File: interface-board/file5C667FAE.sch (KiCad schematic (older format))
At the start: 24 parts

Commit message: interface-board getting there schematic-wise.
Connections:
- net labels added: 12V_IN
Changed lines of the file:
@@
 $Descr A4 11693 8268
 encoding utf-8
-Sheet 4 4
+Sheet 4 5
 Title ""
 Date ""
@@
 Connection ~ 6900 5350
 Text HLabel 8550 3400 0    50   Input ~ 0
-12V_OUT
+12V_IN
 Wire Wire Line
 	8550 3400 8600 3400

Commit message: schematic almost done maybe hopefully
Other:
- note added: "Fix all the HV/LV interface shit"
- moved on the sheet: C?, U?
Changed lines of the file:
@@
 Wire Wire Line
 	5700 3850 5900 3850
-Wire Notes Line
-	3350 4000 3350 2500
 Text Notes 6000 2950 0    50   ~ 0
 Pull high to disable
@@
 Text Notes 4350 2750 0    100  ~ 0
 HV-Interface
-Wire Notes Line width 39 rgb(255, 0, 0)
-	5400 1050 5400 6150
-Text Notes 3500 3800 0    118  ~ 24
+Text Notes 3350 3700 0    118  ~ 24
 HV\nDanger!
 $Comp
@@
 	7400 4750 7400 5800
 Wire Notes Line
-	6000 5800 7300 5800
-Wire Notes Line
-	6100 4750 7400 4750
-Wire Notes Line
 	3300 6200 3300 4650
-Wire Notes Line width 39 rgb(255, 0, 0)
-	5400 1150 3400 1150
 Text Notes 3850 1550 0    50   ~ 0
 May want to change value
@@
 L Regulator_Switching:R-78E5.0-0.5 U?
 U 1 1 5C66BF9B
-P 9050 3400
+P 9000 3550
 AR Path="/5C66BF9B" Ref="U?"  Part="1"
 AR Path="/5C667FAF/5C66BF9B" Ref="U?"  Part="1"
-F 0 "U?" H 9050 3642 50  0000 C CNN
-F 1 "R-78E5.0-0.5" H 9050 3551 50  0000 C CNN
-F 2 "Converter_DCDC:Converter_DCDC_RECOM_R-78E-0.5_THT" H 9100 3150 50  0001 L CIN
-F 3 "https://www.recom-power.com/pdf/Innoline/R-78Exx-0.5.pdf" H 9050 3400 50  0001 C CNN
-	1    9050 3400
-	1    0    0    -1
-$EndComp
-Wire Wire Line
-	8600 3400 8750 3400
-Wire Wire Line
-	9500 3400 9350 3400
+F 0 "U?" H 9000 3792 50  0000 C CNN
+F 1 "R-78E5.0-0.5" H 9000 3701 50  0000 C CNN
+F 2 "Converter_DCDC:Converter_DCDC_RECOM_R-78E-0.5_THT" H 9050 3300 50  0001 L CIN
+F 3 "https://www.recom-power.com/pdf/Innoline/R-78Exx-0.5.pdf" H 9000 3550 50  0001 C CNN
+	1    9000 3550
+	1    0    0    -1
+$EndComp
+Wire Wire Line
+	8550 3550 8700 3550
+Wire Wire Line
+	9450 3550 9300 3550
 $Comp
 L power:GND #PWR?
 U 1 1 5C66BFAA
-P 9050 3750
+P 9000 3900
 AR Path="/5C66BFAA" Ref="#PWR?"  Part="1"
 AR Path="/5C667FAF/5C66BFAA" Ref="#PWR?"  Part="1"
-F 0 "#PWR?" H 9050 3500 50  0001 C CNN
-F 1 "GND" H 9055 3577 50  0000 C CNN
-F 2 "" H 9050 3750 50  0001 C CNN
-F 3 "" H 9050 3750 50  0001 C CNN
-	1    9050 3750
-	1    0    0    -1
-$EndComp
-Wire Wire Line
-	9050 3750 9050 3700
-Wire Notes Line
-	8100 4050 8100 2750
-Text Notes 8150 2900 0    100  ~ 0
+F 0 "#PWR?" H 9000 3650 50  0001 C CNN
+F 1 "GND" H 9005 3727 50  0000 C CNN
+F 2 "" H 9000 3900 50  0001 C CNN
+F 3 "" H 9000 3900 50  0001 C CNN
+	1    9000 3900
+	1    0    0    -1
+$EndComp
+Wire Wire Line
+	9000 3900 9000 3850
+Text Notes 8100 3050 0    100  ~ 0
 12V->5V
 $Comp
 L Device:C C?
 U 1 1 5C66BFB3
-P 9500 3550
+P 9450 3700
 AR Path="/5C66BFB3" Ref="C?"  Part="1"
 AR Path="/5C667FAF/5C66BFB3" Ref="C?"  Part="1"
-F 0 "C?" H 9615 3596 50  0000 L CNN
-F 1 "0.1uF" H 9250 3450 50  0000 L CNN
-F 2 "Capacitor_SMD:C_0603_1608Metric" H 9538 3400 50  0001 C CNN
-F 3 "~" H 9500 3550 50  0001 C CNN
-	1    9500 3550
-	1    0    0    -1
-$EndComp
-Connection ~ 9500 3400
+F 0 "C?" H 9565 3746 50  0000 L CNN
+F 1 "0.1uF" H 9200 3600 50  0000 L CNN
+F 2 "Capacitor_SMD:C_0603_1608Metric" H 9488 3550 50  0001 C CNN
+F 3 "~" H 9450 3700 50  0001 C CNN
+	1    9450 3700
+	1    0    0    -1
+$EndComp
+Connection ~ 9450 3550
 $Comp
 L power:GND #PWR?
 U 1 1 5C66BFC5
-P 9650 3750
+P 9600 3900
 AR Path="/5C66BFC5" Ref="#PWR?"  Part="1"
 AR Path="/5C667FAF/5C66BFC5" Ref="#PWR?"  Part="1"
-F 0 "#PWR?" H 9650 3500 50  0001 C CNN
-F 1 "GND" H 9655 3577 50  0000 C CNN
-F 2 "" H 9650 3750 50  0001 C CNN
-F 3 "" H 9650 3750 50  0001 C CNN
-	1    9650 3750
-	1    0    0    -1
-$EndComp
-Wire Wire Line
-	9500 3700 9650 3700
-Wire Wire Line
-	9650 3700 9650 3750
-Connection ~ 9650 3700
-Wire Wire Line
-	9650 3700 9800 3700
+F 0 "#PWR?" H 9600 3650 50  0001 C CNN
+F 1 "GND" H 9605 3727 50  0000 C CNN
+F 2 "" H 9600 3900 50  0001 C CNN
+F 3 "" H 9600 3900 50  0001 C CNN
+	1    9600 3900
+	1    0    0    -1
+$EndComp
+Wire Wire Line
+	9450 3850 9600 3850
+Wire Wire Line
+	9600 3850 9600 3900
+Connection ~ 9600 3850
+Wire Wire Line
+	9600 3850 9750 3850
 $Comp
 L Device:C C?
 U 1 1 5C66BFCF
-P 8600 3550
+P 8550 3700
 AR Path="/5C66BFCF" Ref="C?"  Part="1"
 AR Path="/5C667FAF/5C66BFCF" Ref="C?"  Part="1"
-F 0 "C?" H 8715 3596 50  0000 L CNN
-F 1 "10uF" H 8715 3505 50  0000 L CNN
-F 2 "Capacitor_SMD:C_0603_1608Metric" H 8638 3400 50  0001 C CNN
-F 3 "~" H 8600 3550 50  0001 C CNN
-	1    8600 3550
+F 0 "C?" H 8665 3746 50  0000 L CNN
+F 1 "10uF" H 8665 3655 50  0000 L CNN
+F 2 "Capacitor_SMD:C_0603_1608Metric" H 8588 3550 50  0001 C CNN
+F 3 "~" H 8550 3700 50  0001 C CNN
+	1    8550 3700
 	1    0    0    -1
 $EndComp
@@
 L power:GND #PWR?
 U 1 1 5C66BFD7
-P 8600 3700
+P 8550 3850
 AR Path="/5C66BFD7" Ref="#PWR?"  Part="1"
 AR Path="/5C667FAF/5C66BFD7" Ref="#PWR?"  Part="1"
-F 0 "#PWR?" H 8600 3450 50  0001 C CNN
-F 1 "GND" H 8605 3527 50  0000 C CNN
-F 2 "" H 8600 3700 50  0001 C CNN
-F 3 "" H 8600 3700 50  0001 C CNN
-	1    8600 3700
-	1    0    0    -1
-$EndComp
-Wire Notes Line
-	10200 2750 10200 4050
-Wire Notes Line
-	8400 4050 10150 4050
-Wire Notes Line
-	8400 2750 10150 2750
+F 0 "#PWR?" H 8550 3600 50  0001 C CNN
+F 1 "GND" H 8555 3677 50  0000 C CNN
+F 2 "" H 8550 3850 50  0001 C CNN
+F 3 "" H 8550 3850 50  0001 C CNN
+	1    8550 3850
+	1    0    0    -1
+$EndComp
+Wire Notes Line
+	10150 2900 10150 4200
 Text HLabel 6200 1650 2    50   Input ~ 0
 TRIM_EN
@@
 	3600 5700 4100 5700
 Connection ~ 4100 5700
-Wire Notes Line
-	3350 5100 4450 5100
-Wire Notes Line
-	3350 6150 4450 6150
 Connection ~ 4400 5500
 Connection ~ 4400 5700
-Wire Notes Line width 39 rgb(255, 0, 0)
-	3250 1150 3250 6250
 Wire Wire Line
 	4400 5500 4950 5500
@@
 	4600 5200 4950 5200
 Wire Notes Line
-	3550 6200 7350 6200
-Wire Notes Line
 	7450 4650 7450 6200
-Wire Notes Line
-	3650 4650 7450 4650
 Text HLabel 6950 5350 2    50   Input ~ 0
 12V_OUT
@@
 	6900 5350 6950 5350
 Connection ~ 6900 5350
-Text HLabel 8550 3400 0    50   Input ~ 0
+Text HLabel 8500 3550 0    50   Input ~ 0
 12V_IN
 Wire Wire Line
-	8550 3400 8600 3400
-Connection ~ 8600 3400
-Wire Wire Line
-	9800 3400 9500 3400
+	8500 3550 8550 3550
+Connection ~ 8550 3550
+Wire Wire Line
+	9750 3550 9450 3550
 $Comp
 L Device:C C?
 U 1 1 5C66BFBA
-P 9800 3550
+P 9750 3700
 AR Path="/5C66BFBA" Ref="C?"  Part="1"
 AR Path="/5C667FAF/5C66BFBA" Ref="C?"  Part="1"
-F 0 "C?" H 9915 3596 50  0000 L CNN
-F 1 "10uF" H 9915 3505 50  0000 L CNN
-F 2 "Capacitor_SMD:C_0603_1608Metric" H 9838 3400 50  0001 C CNN
-F 3 "~" H 9800 3550 50  0001 C CNN
-	1    9800 3550
-	1    0    0    -1
-$EndComp
-Text HLabel 9850 3400 2    50   Input ~ 0
+F 0 "C?" H 9865 3746 50  0000 L CNN
+F 1 "10uF" H 9865 3655 50  0000 L CNN
+F 2 "Capacitor_SMD:C_0603_1608Metric" H 9788 3550 50  0001 C CNN
+F 3 "~" H 9750 3700 50  0001 C CNN
+	1    9750 3700
+	1    0    0    -1
+$EndComp
+Text HLabel 9800 3550 2    50   Input ~ 0
 5V_OUT
 Wire Wire Line
-	9850 3400 9800 3400
-Connection ~ 9800 3400
+	9800 3550 9750 3550
+Connection ~ 9750 3550
+Wire Notes Line
+	3300 4650 7450 4650
+Wire Notes Line
+	3300 6200 7450 6200
+Wire Notes Line
+	6000 4750 7400 4750
+Wire Notes Line
+	6000 5800 7400 5800
+Wire Notes Line
+	3350 5100 4500 5100
+Wire Notes Line
+	3350 6150 4500 6150
+Wire Notes Line
+	3350 6150 3350 5100
+Wire Notes Line
+	8050 4200 10150 4200
+Wire Notes Line
+	8050 2900 8050 4200
+Wire Notes Line
+	8050 2900 10150 2900
+Wire Notes Line width 39 rgb(253, 0, 1)
+	3150 1150 5400 1150
+Wire Notes Line width 39 rgb(255, 0, 0)
+	5400 1150 5400 6300
+Wire Notes Line width 39 rgb(253, 0, 0)
+	5400 6300 3150 6300
+Wire Notes Line width 39 rgb(255, 0, 0)
+	3150 1150 3150 6300
+Text Notes 3550 1000 0    157  ~ 31
+Fix all the HV/LV interface shit
 $EndSCHEMATC

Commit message: more interface-board
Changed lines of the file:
@@
 Wire Notes Line
 	3300 6200 3300 4650
-Text Notes 3850 1550 0    50   ~ 0
+Text Notes 1150 1750 0    157  ~ 31
 May want to change value
 $Comp

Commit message: Beginnings of board layout of interface-board
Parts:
- gave numbers to parts that had none: 23

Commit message: Getting there with layout of big board...
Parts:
- removed U4: LTV-827S, Package_DIP:SMDIP-8_W9.53mm, symbol Isolator:LTV-827S
- removed U6: LTV-824, Package_DIP:DIP-8_W7.62mm, symbol Isolator:LTV-824
- added U4, U6: LTV-817S, Package_DIP:SMDIP-4_W9.53mm, symbol Isolator:LTV-817S
- added U9: TLP184, CustomFootprints:TLP182, symbol Isolator:TLP184
- R18: value 50k -> 6.8k
- RV1: value 5k -> 50k; footprint Potentiometer_THT:Potentiometer_Piher_PT-15-V02_Vertical -> CustomFootprints:TC33X-503ECT-ND
- U5: footprint CustomFootprints:DCM4623TD2J13D0T70 w_landpattern -> CustomFootprints:DCM4623TD2J13D0T70_w_landpattern
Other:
- note removed: "May want to change value"
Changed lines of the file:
@@
 F 0 "U5" H 5375 5925 50  0000 C CNN
 F 1 "DCM4623TD2J13D0T70" H 5375 5834 50  0000 C CNN
-F 2 "CustomFootprints:DCM4623TD2J13D0T70 w_landpattern" H 5350 5400 50  0001 C CNN
+F 2 "CustomFootprints:DCM4623TD2J13D0T70_w_landpattern" H 5350 5400 50  0001 C CNN
 F 3 "" H 5350 5400 50  0001 C CNN
 	1    5350 5400
@@
 	0    1    1    0
 $EndComp
-$Comp
-L Device:R_US R?
-U 1 1 5C66882C
-P 4800 4000
-AR Path="/5C66882C" Ref="R?"  Part="1"
-AR Path="/5C667FAF/5C66882C" Ref="R18"  Part="1"
-F 0 "R18" H 4650 4050 50  0000 L CNN
-F 1 "50k" H 4550 3950 50  0000 L CNN
-F 2 "Resistor_SMD:R_0603_1608Metric" V 4840 3990 50  0001 C CNN
-F 3 "~" H 4800 4000 50  0001 C CNN
-	1    4800 4000
-	1    0    0    -1
-$EndComp
 Text Label 4350 3850 0    50   ~ 0
 FAULT_HV
@@
 AR Path="/5C667FAF/5C668874" Ref="RV1"  Part="1"
 F 0 "RV1" H 4382 1846 50  0000 R CNN
-F 1 "5k" H 4382 1755 50  0000 R CNN
-F 2 "Potentiometer_THT:Potentiometer_Piher_PT-15-V02_Vertical" H 4450 1800 50  0001 C CNN
+F 1 "50k" H 4382 1755 50  0000 R CNN
+F 2 "CustomFootprints:TC33X-503ECT-ND" H 4450 1800 50  0001 C CNN
 F 3 "~" H 4450 1800 50  0001 C CNN
 	1    4450 1800
@@
 Wire Notes Line
 	3300 6200 3300 4650
-Text Notes 1150 1750 0    157  ~ 31
-May want to change value
-$Comp
-L Isolator:LTV-827S U?
-U 1 1 5C6688F6
-P 5350 1750
-AR Path="/5C6688F6" Ref="U?"  Part="1"
-AR Path="/5C667FAF/5C6688F6" Ref="U4"  Part="1"
-F 0 "U4" H 5350 2075 50  0000 C CNN
-F 1 "LTV-827S" H 5350 1984 50  0000 C CNN
-F 2 "Package_DIP:SMDIP-8_W9.53mm" H 5350 1450 50  0001 C CNN
-F 3 "http://www.us.liteon.com/downloads/LTV-817-827-847.PDF" H 4550 2300 50  0001 C CNN
-	1    5350 1750
-	-1   0    0    -1
-$EndComp
 Wire Wire Line
 	5700 4050 5700 4200
-$Comp
-L Isolator:LTV-824 U?
-U 1 1 5C6688FE
-P 5400 3150
-AR Path="/5C6688FE" Ref="U?"  Part="1"
-AR Path="/5C667FAF/5C6688FE" Ref="U6"  Part="1"
-F 0 "U6" H 5400 3475 50  0000 C CNN
-F 1 "LTV-824" H 5400 3384 50  0000 C CNN
-F 2 "Package_DIP:DIP-8_W7.62mm" H 5200 2950 50  0001 L CIN
-F 3 "http://optoelectronics.liteon.com/upload/download/DS-70-96-0013/S_110_LTV-814%20824%20844%20(M,%20S,%20S-TA,%20S-TA1,%20S-TP)%20Series.pdf" H 5425 3150 50  0001 L CNN
-	1    5400 3150
-	1    0    0    -1
-$EndComp
-$Comp
-L Isolator:LTV-824 U?
-U 2 1 5C668905
-P 5400 3950
-AR Path="/5C668905" Ref="U?"  Part="2"
-AR Path="/5C667FAF/5C668905" Ref="U6"  Part="2"
-F 0 "U6" H 5400 3633 50  0000 C CNN
-F 1 "LTV-824" H 5400 3724 50  0000 C CNN
-F 2 "Package_DIP:DIP-8_W7.62mm" H 5200 3750 50  0001 L CIN
-F 3 "http://optoelectronics.liteon.com/upload/download/DS-70-96-0013/S_110_LTV-814%20824%20844%20(M,%20S,%20S-TA,%20S-TA1,%20S-TP)%20Series.pdf" H 5425 3950 50  0001 L CNN
-	2    5400 3950
-	1    0    0    1
-$EndComp
 Wire Wire Line
 	4350 3850 4800 3850
-Connection ~ 4800 3850
 $Comp
 L Regulator_Switching:R-78E5.0-0.5 U?
@@
 Wire Wire Line
 	5050 3250 5100 3250
-Wire Wire Line
-	4800 4150 5050 4150
 Text HLabel 5050 4150 3    50   Input ~ 0
 HV-
-Text HLabel 4250 1850 3    50   Input ~ 0
+Text HLabel 3900 1850 3    50   Input ~ 0
 HV-
-Wire Wire Line
-	4250 1800 4250 1850
 Wire Wire Line
 	4850 3050 5100 3050
@@
 Text Notes 3550 1000 0    157  ~ 31
 Fix all the HV/LV interface shit
+$Comp
+L Device:R_US R18
+U 1 1 5C602E65
+P 4100 1800
+F 0 "R18" V 3895 1800 50  0000 C CNN
+F 1 "6.8k" V 3986 1800 50  0000 C CNN
+F 2 "Resistor_SMD:R_0603_1608Metric" V 4140 1790 50  0001 C CNN
+F 3 "~" H 4100 1800 50  0001 C CNN
+	1    4100 1800
+	0    1    1    0
+$EndComp
+Wire Wire Line
+	3900 1850 3900 1800
+Wire Wire Line
+	3900 1800 3950 1800
+$Comp
+L Isolator:LTV-817S U4
+U 1 1 5C6049E0
+P 5350 1750
+F 0 "U4" H 5350 2075 50  0000 C CNN
+F 1 "LTV-817S" H 5350 1984 50  0000 C CNN
+F 2 "Package_DIP:SMDIP-4_W9.53mm" H 5350 1450 50  0001 C CNN
+F 3 "http://www.us.liteon.com/downloads/LTV-817-827-847.PDF" H 5000 2050 50  0001 C CNN
+	1    5350 1750
+	-1   0    0    -1
+$EndComp
+$Comp
+L Isolator:LTV-817S U6
+U 1 1 5C60528B
+P 5400 3150
+F 0 "U6" H 5400 3475 50  0000 C CNN
+F 1 "LTV-817S" H 5400 3384 50  0000 C CNN
+F 2 "Package_DIP:SMDIP-4_W9.53mm" H 5400 2850 50  0001 C CNN
+F 3 "http://www.us.liteon.com/downloads/LTV-817-827-847.PDF" H 5050 3450 50  0001 C CNN
+	1    5400 3150
+	-1   0    0    -1
+$EndComp
+$Comp
+L Isolator:TLP184 U9
+U 1 1 5C60549B
+P 5400 3950
+F 0 "U9" H 5400 4275 50  0000 C CNN
+F 1 "TLP184" H 5400 4184 50  0000 C CNN
+F 2 "CustomFootprints:TLP182" H 5400 3650 50  0001 C CIN
+F 3 "https://toshiba.semicon-storage.com/info/docget.jsp?did=11793&prodName=TLP184" H 5450 3950 50  0001 L CNN
+	1    5400 3950
+	1    0    0    -1
+$EndComp
 $EndSCHEMATC

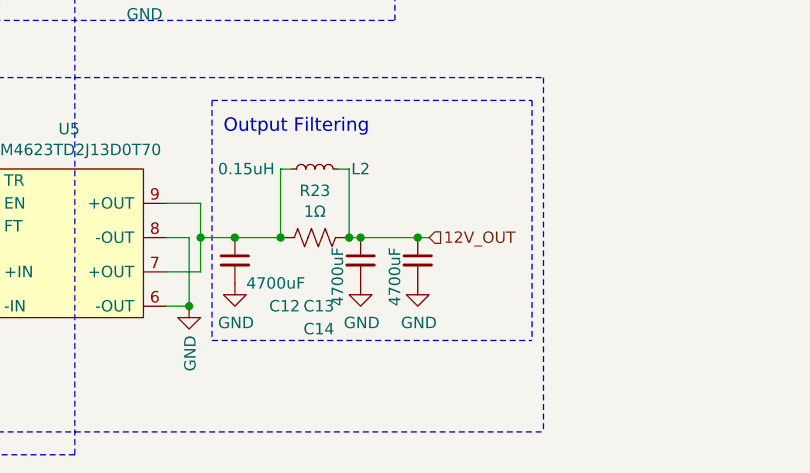
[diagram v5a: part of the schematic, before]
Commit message: Interface-board largely routed
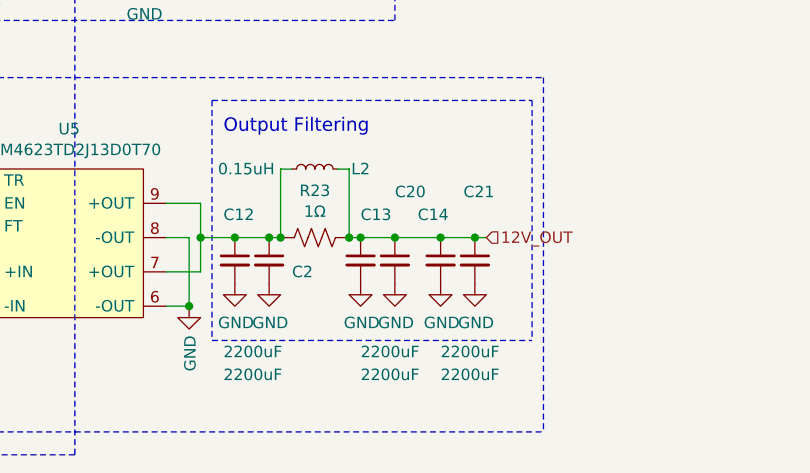
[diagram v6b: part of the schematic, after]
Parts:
- added C2, C20, C21: 2200uF, Capacitor_THT:CP_Radial_D18.0mm_P7.50mm, symbol Device:C_Small
- C12, C13, C14: value 4700uF -> 2200uF
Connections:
- net 12V_OUT: now also C20.1, C21.1
- net GND: now also C2.2, C20.2, C21.2
- net at C12.1, L2.1, R23.2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: now also C2.1
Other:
- moved on the sheet: C14
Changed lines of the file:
@@
 AR Path="/5C6688A6" Ref="C?"  Part="1"
 AR Path="/5C667FAF/5C6688A6" Ref="C12"  Part="1"
-F 0 "C12" H 6250 5250 50  0000 L CNN
-F 1 "4700uF" H 6150 5350 50  0000 L CNN
+F 0 "C12" H 6050 5650 50  0000 L CNN
+F 1 "2200uF" H 6050 5050 50  0000 L CNN
 F 2 "Capacitor_THT:CP_Radial_D18.0mm_P7.50mm" H 6100 5450 50  0001 C CNN
 F 3 "~" H 6100 5450 50  0001 C CNN
@@
 	5950 5350 5950 5500
 Wire Wire Line
-	6100 5350 6300 5350
+	6100 5350 6250 5350
 Connection ~ 6100 5350
 Wire Wire Line
@@
 AR Path="/5C6688C3" Ref="C?"  Part="1"
 AR Path="/5C667FAF/5C6688C3" Ref="C13"  Part="1"
-F 0 "C13" H 6400 5250 50  0000 L CNN
-F 1 "4700uF" V 6550 5250 50  0000 L CNN
+F 0 "C13" H 6650 5650 50  0000 L CNN
+F 1 "2200uF" H 6650 5050 50  0000 L CNN
 F 2 "Capacitor_THT:CP_Radial_D18.0mm_P7.50mm" H 6650 5450 50  0001 C CNN
 F 3 "~" H 6650 5450 50  0001 C CNN
@@
 L Device:C_Small C?
 U 1 1 5C6688CA
-P 6900 5450
+P 7000 5450
 AR Path="/5C6688CA" Ref="C?"  Part="1"
 AR Path="/5C667FAF/5C6688CA" Ref="C14"  Part="1"
-F 0 "C14" H 6400 5150 50  0000 L CNN
-F 1 "4700uF" V 6800 5250 50  0000 L CNN
-F 2 "Capacitor_THT:CP_Radial_D18.0mm_P7.50mm" H 6900 5450 50  0001 C CNN
-F 3 "~" H 6900 5450 50  0001 C CNN
-	1    6900 5450
+F 0 "C14" H 6900 5650 50  0000 L CNN
+F 1 "2200uF" H 7000 5050 50  0000 L CNN
+F 2 "Capacitor_THT:CP_Radial_D18.0mm_P7.50mm" H 7000 5450 50  0001 C CNN
+F 3 "~" H 7000 5450 50  0001 C CNN
+	1    7000 5450
 	1    0    0    -1
 $EndComp
@@
 Connection ~ 6600 5350
 Connection ~ 6650 5350
-Wire Wire Line
-	6650 5350 6900 5350
 $Comp
 L power:GND #PWR?
@@
 L power:GND #PWR?
 U 1 1 5C6688DB
-P 6900 5550
+P 7000 5550
 AR Path="/5C6688DB" Ref="#PWR?"  Part="1"
 AR Path="/5C667FAF/5C6688DB" Ref="#PWR064"  Part="1"
-F 0 "#PWR064" H 6900 5300 50  0001 C CNN
-F 1 "GND" H 6905 5377 50  0000 C CNN
-F 2 "" H 6900 5550 50  0001 C CNN
-F 3 "" H 6900 5550 50  0001 C CNN
-	1    6900 5550
+F 0 "#PWR064" H 7000 5300 50  0001 C CNN
+F 1 "GND" H 7005 5377 50  0000 C CNN
+F 2 "" H 7000 5550 50  0001 C CNN
+F 3 "" H 7000 5550 50  0001 C CNN
+	1    7000 5550
 	1    0    0    -1
 $EndComp
@@
 Wire Notes Line
 	7450 4650 7450 6200
-Text HLabel 6950 5350 2    50   Input ~ 0
+Text HLabel 7200 5350 2    50   Input ~ 0
 12V_OUT
-Wire Wire Line
-	6900 5350 6950 5350
-Connection ~ 6900 5350
 Text HLabel 8500 3550 0    50   Input ~ 0
 12V_IN
@@
 	1    0    0    -1
 $EndComp
+$Comp
+L Device:C_Small C?
+U 1 1 5C609387
+P 6250 5450
+AR Path="/5C609387" Ref="C?"  Part="1"
+AR Path="/5C667FAF/5C609387" Ref="C2"  Part="1"
+F 0 "C2" H 6350 5400 50  0000 L CNN
+F 1 "2200uF" H 6050 4950 50  0000 L CNN
+F 2 "Capacitor_THT:CP_Radial_D18.0mm_P7.50mm" H 6250 5450 50  0001 C CNN
+F 3 "~" H 6250 5450 50  0001 C CNN
+	1    6250 5450
+	1    0    0    -1
+$EndComp
+Connection ~ 6250 5350
+Wire Wire Line
+	6250 5350 6300 5350
+$Comp
+L power:GND #PWR?
+U 1 1 5C6093CD
+P 6250 5550
+AR Path="/5C6093CD" Ref="#PWR?"  Part="1"
+AR Path="/5C667FAF/5C6093CD" Ref="#PWR0107"  Part="1"
+F 0 "#PWR0107" H 6250 5300 50  0001 C CNN
+F 1 "GND" H 6255 5377 50  0000 C CNN
+F 2 "" H 6250 5550 50  0001 C CNN
+F 3 "" H 6250 5550 50  0001 C CNN
+	1    6250 5550
+	1    0    0    -1
+$EndComp
+$Comp
+L Device:C_Small C?
+U 1 1 5C60950B
+P 7150 5450
+AR Path="/5C60950B" Ref="C?"  Part="1"
+AR Path="/5C667FAF/5C60950B" Ref="C21"  Part="1"
+F 0 "C21" H 7100 5750 50  0000 L CNN
+F 1 "2200uF" H 7000 4950 50  0000 L CNN
+F 2 "Capacitor_THT:CP_Radial_D18.0mm_P7.50mm" H 7150 5450 50  0001 C CNN
+F 3 "~" H 7150 5450 50  0001 C CNN
+	1    7150 5450
+	1    0    0    -1
+$EndComp
+$Comp
+L power:GND #PWR?
+U 1 1 5C609512
+P 7150 5550
+AR Path="/5C609512" Ref="#PWR?"  Part="1"
+AR Path="/5C667FAF/5C609512" Ref="#PWR0108"  Part="1"
+F 0 "#PWR0108" H 7150 5300 50  0001 C CNN
+F 1 "GND" H 7155 5377 50  0000 C CNN
+F 2 "" H 7150 5550 50  0001 C CNN
+F 3 "" H 7150 5550 50  0001 C CNN
+	1    7150 5550
+	1    0    0    -1
+$EndComp
+$Comp
+L Device:C_Small C?
+U 1 1 5C60ACA7
+P 6800 5450
+AR Path="/5C60ACA7" Ref="C?"  Part="1"
+AR Path="/5C667FAF/5C60ACA7" Ref="C20"  Part="1"
+F 0 "C20" H 6800 5750 50  0000 L CNN
+F 1 "2200uF" H 6650 4950 50  0000 L CNN
+F 2 "Capacitor_THT:CP_Radial_D18.0mm_P7.50mm" H 6800 5450 50  0001 C CNN
+F 3 "~" H 6800 5450 50  0001 C CNN
+	1    6800 5450
+	1    0    0    -1
+$EndComp
+$Comp
+L power:GND #PWR?
+U 1 1 5C60ACAE
+P 6800 5550
+AR Path="/5C60ACAE" Ref="#PWR?"  Part="1"
+AR Path="/5C667FAF/5C60ACAE" Ref="#PWR0109"  Part="1"
+F 0 "#PWR0109" H 6800 5300 50  0001 C CNN
+F 1 "GND" H 6805 5377 50  0000 C CNN
+F 2 "" H 6800 5550 50  0001 C CNN
+F 3 "" H 6800 5550 50  0001 C CNN
+	1    6800 5550
+	1    0    0    -1
+$EndComp
+Connection ~ 7000 5350
+Wire Wire Line
+	7000 5350 7150 5350
+Connection ~ 7150 5350
+Wire Wire Line
+	7150 5350 7200 5350
+Wire Wire Line
+	6650 5350 6800 5350
+Connection ~ 6800 5350
+Wire Wire Line
+	6800 5350 7000 5350
 $EndSCHEMATC

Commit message: Cleaned up 3d models
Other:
- note removed: "Fix all the HV/LV interface shit"
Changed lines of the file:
@@
 Wire Notes Line width 39 rgb(255, 0, 0)
 	3150 1150 3150 6300
-Text Notes 3550 1000 0    157  ~ 31
-Fix all the HV/LV interface shit
 $Comp
 L Device:R_US R18
